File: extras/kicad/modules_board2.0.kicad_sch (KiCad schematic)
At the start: 31 parts, among them J1 CONN_08NO_SILK_FEMALE_PTH, J10 CONN_06LOCK, J12 CONN_06LOCK, J13 CONN_06LOCK, J2 CONN_08NO_SILK_FEMALE_PTH, J3 CONN_08NO_SILK_FEMALE_PTH, J4 CONN_08NO_SILK_FEMALE_PTH, J9 CONN_06LOCK

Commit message: Add files via upload
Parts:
- removed J10, J12, J13, J9: CONN_06LOCK, modules_board:1X06_LOCK, symbol modules_board-eagle-import:CONN_06LOCK
- removed J?: UEXT_Slave, symbol Connector:UEXT_Slave
- removed UNK5V_REGULATOR0: CONN_03LOCK, modules_board:1X03_LOCK, symbol modules_board-eagle-import:CONN_03LOCK
- added J?: Conn_02x08_Odd_Even, symbol Connector_Generic:Conn_02x08_Odd_Even
- added J? (x4): Conn_01x04_Male, symbol Connector:Conn_01x04_Male
- added J? (x5): Conn_01x05_Male, symbol Connector:Conn_01x05_Male
- added J?: Conn_01x07_Male, symbol Connector:Conn_01x07_Male
- added J?: UEXT_Slave, symbol Connector:UEXT_Slave
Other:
- note added: "3amp @5v"
- note added: "Breakout garden SPI"
- note added: "Featherwing Breakout - UART I2C & SPI"
- note added: "Grove I2C"
- note added: "Qwiic I2C"
- note added: "https://shop.pimoroni.com/collections/breakout-garden"
- note added: "https://www.adafruit.com/category/573"
- note added: "https://www.mikroe.com/mikrobus-shuttle-127mm-2x8-pin-box-header-smd-male"
- note added: "mikroMOD"

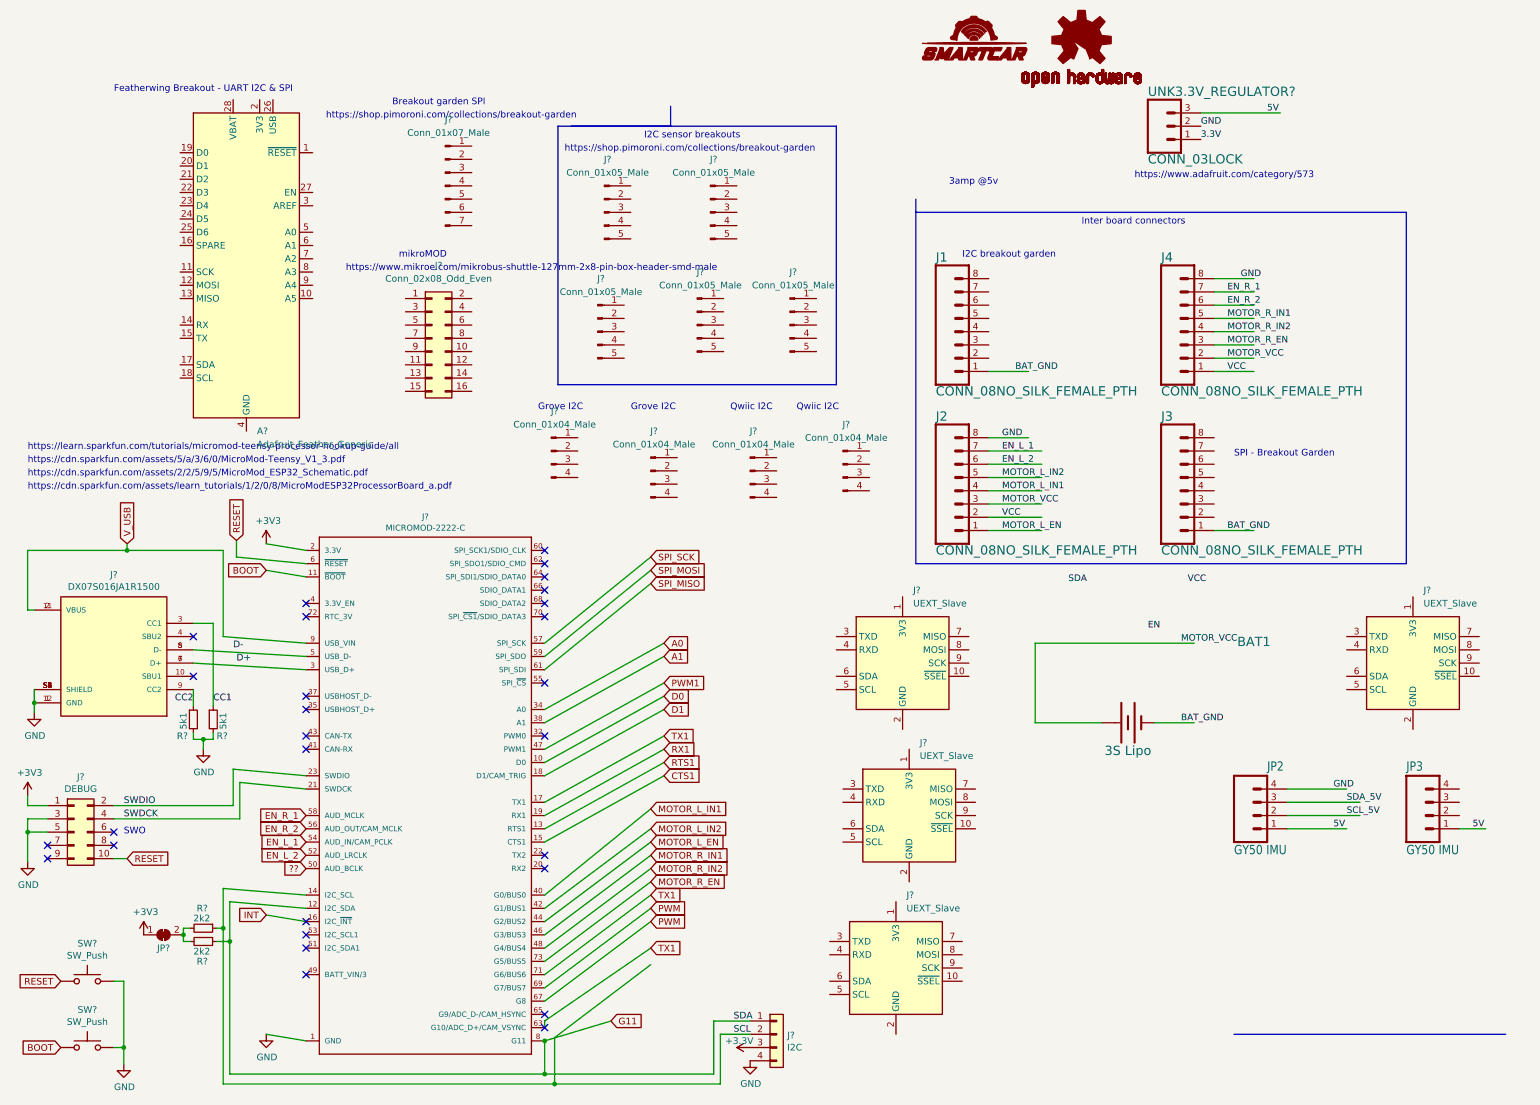
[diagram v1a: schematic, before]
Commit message: Add BNO-85
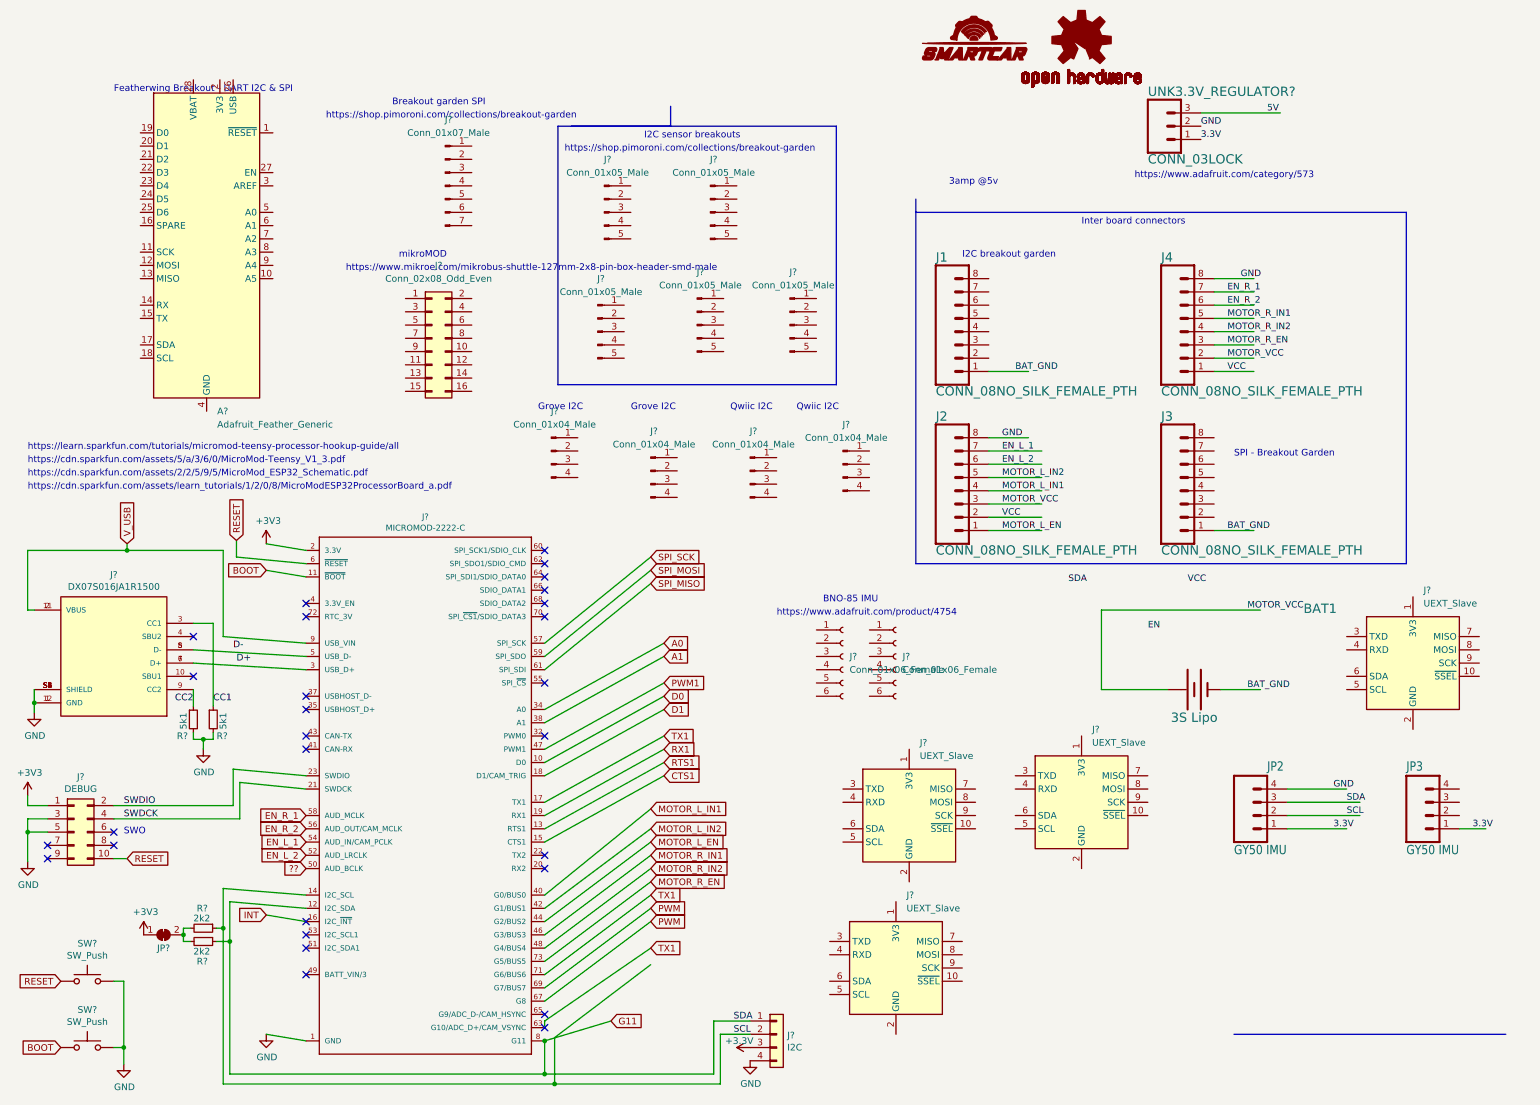
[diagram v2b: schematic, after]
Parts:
- added J? (x2): Conn_01x06_Female, symbol Connector:Conn_01x06_Female
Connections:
- net SCL_5V is gone; now on net SCL: JP2.2
- net SDA_5V is gone; now on net G11: JP2.3
- net +3V3: now also JP2.1, JP3.1
- net 5V: no longer JP2.1, JP3.1
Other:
- note added: "BNO-85 IMU"
- note added: "https://www.adafruit.com/product/4754"
- moved on the sheet: A?, BAT1, J?
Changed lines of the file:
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@@
     (stroke (width 0) (type default) (color 0 0 0 0))
   )
-  (wire (pts (xy 207.01 135.89) (xy 219.71 135.89))
+  (wire (pts (xy 219.71 129.54) (xy 232.41 129.54))
     (stroke (width 0) (type default) (color 0 0 0 0))
   )
@@
     (stroke (width 0) (type default) (color 0 0 0 0))
   )
-  (wire (pts (xy 207.01 120.65) (xy 237.49 120.65))
+  (wire (pts (xy 219.71 114.3) (xy 250.19 114.3))
     (stroke (width 0) (type default) (color 0 0 0 0))
   )
@@
     (stroke (width 0) (type default) (color 0 0 0 0))
   )
-  (wire (pts (xy 229.87 135.89) (xy 237.49 135.89))
+  (wire (pts (xy 242.57 129.54) (xy 250.19 129.54))
     (stroke (width 0) (type default) (color 0 0 0 0))
   )
@@
     (stroke (width 0) (type default) (color 0 0 0 0))
   )
-  (wire (pts (xy 207.01 120.65) (xy 207.01 135.89))
+  (wire (pts (xy 219.71 114.3) (xy 219.71 129.54))
     (stroke (width 0) (type default) (color 0 0 0 0))
   )
@@
     (effects (font (size 1.27 1.27)) (justify left bottom))
   )
+  (text "BNO-85 IMU" (at 166.37 113.03 0)
+    (effects (font (size 1.27 1.27)) (justify left bottom))
+  )
   (text "Inter board connectors" (at 215.9 40.64 0)
     (effects (font (size 1.27 1.27)) (justify left bottom))
@@
     (effects (font (size 1.27 1.27)) (justify left bottom))
   )
+  (text "https://www.adafruit.com/product/4754" (at 157.48 115.57 0)
+    (effects (font (size 1.27 1.27)) (justify left bottom))
+  )
   (label "VCC" (at 236.22 109.22 0)
     (effects (font (size 1.2446 1.2446)) (justify left bottom))
@@
     (effects (font (size 1.2446 1.2446)) (justify left bottom))
   )
-  (label "SDA_5V" (at 266.7 151.13 0)
+  (label "SDA" (at 266.7 151.13 0)
     (effects (font (size 1.2446 1.2446)) (justify left bottom))
   )
@@
     (effects (font (size 1.27 1.27)) (justify left bottom))
   )
-  (label "5V" (at 264.16 156.21 0)
+  (label "3.3V" (at 264.16 156.21 0)
     (effects (font (size 1.2446 1.2446)) (justify left bottom))
   )
@@
     (effects (font (size 1.2446 1.2446)) (justify left bottom))
   )
-  (label "BAT_GND" (at 234.95 135.89 0)
-    (effects (font (size 1.2446 1.2446)) (justify left bottom))
-  )
-  (label "5V" (at 290.83 156.21 0)
+  (label "BAT_GND" (at 247.65 129.54 0)
+    (effects (font (size 1.2446 1.2446)) (justify left bottom))
+  )
+  (label "3.3V" (at 290.83 156.21 0)
     (effects (font (size 1.2446 1.2446)) (justify left bottom))
   )
@@
     (effects (font (size 1.2446 1.2446)) (justify left bottom))
   )
-  (label "MOTOR_VCC" (at 234.95 120.65 0)
+  (label "MOTOR_VCC" (at 247.65 114.3 0)
     (effects (font (size 1.2446 1.2446)) (justify left bottom))
   )
@@
     (effects (font (size 1.27 1.27)) (justify right bottom))
   )
-  (label "SCL_5V" (at 266.7 153.67 0)
+  (label "SCL" (at 266.7 153.67 0)
     (effects (font (size 1.2446 1.2446)) (justify left bottom))
   )
@@
     )
   )
-  (symbol (lib_id "modules_board-eagle-import:AA-BATTERY-PTH") (at 224.79 135.89 0) (unit 1)
-    (in_bom yes) (on_board yes)
-    (property "Reference" "BAT1" (id 0) (at 248.92 121.412 0)
+  (symbol (lib_id "modules_board-eagle-import:AA-BATTERY-PTH") (at 237.49 129.54 0) (unit 1)
+    (in_bom yes) (on_board yes)
+    (property "Reference" "BAT1" (id 0) (at 261.62 115.062 0)
       (effects (font (size 1.778 1.778)) (justify bottom))
     )
-    (property "Value" "3S Lipo" (id 1) (at 224.79 140.208 0)
+    (property "Value" "3S Lipo" (id 1) (at 237.49 133.858 0)
       (effects (font (size 1.778 1.778)) (justify top))
     )
-    (property "Footprint" "modules_board:AA-PCB-BATTERY" (id 2) (at 224.79 135.89 0)
-      (effects (font (size 1.27 1.27)) hide)
-    )
-    (property "Datasheet" "" (id 3) (at 224.79 135.89 0)
+    (property "Footprint" "modules_board:AA-PCB-BATTERY" (id 2) (at 237.49 129.54 0)
+      (effects (font (size 1.27 1.27)) hide)
+    )
+    (property "Datasheet" "" (id 3) (at 237.49 129.54 0)
       (effects (font (size 1.27 1.27)) hide)
     )
@@
     (pin "S6")
   )
-  (symbol (lib_id "Connector:UEXT_Slave") (at 181.61 124.46 0) (unit 1)
+  (symbol (lib_id "Connector:UEXT_Slave") (at 215.9 151.13 0) (unit 1)
     (in_bom yes) (on_board yes) (fields_autoplaced)
-    (property "Reference" "J?" (id 0) (at 183.6294 110.49 0)
-      (effects (font (size 1.27 1.27)) (justify left))
-    )
-    (property "Value" "UEXT_Slave" (id 1) (at 183.6294 113.03 0)
-      (effects (font (size 1.27 1.27)) (justify left))
-    )
-    (property "Footprint" "" (id 2) (at 177.8 124.46 0)
-      (effects (font (size 1.27 1.27)) hide)
-    )
-    (property "Datasheet" "https://www.olimex.com/Products/Modules/UEXT/resources/UEXT_rev_B.pdf" (id 3) (at 177.8 124.46 0)
+    (property "Reference" "J?" (id 0) (at 217.9194 137.16 0)
+      (effects (font (size 1.27 1.27)) (justify left))
+    )
+    (property "Value" "UEXT_Slave" (id 1) (at 217.9194 139.7 0)
+      (effects (font (size 1.27 1.27)) (justify left))
+    )
+    (property "Footprint" "" (id 2) (at 212.09 151.13 0)
+      (effects (font (size 1.27 1.27)) hide)
+    )
+    (property "Datasheet" "https://www.olimex.com/Products/Modules/UEXT/resources/UEXT_rev_B.pdf" (id 3) (at 212.09 151.13 0)
       (effects (font (size 1.27 1.27)) hide)
     )
@@
     (pin "1")
     (pin "2")
+  )
+  (symbol (lib_id "Connector:Conn_01x06_Female") (at 170.18 123.19 0) (unit 1)
+    (in_bom yes) (on_board yes) (fields_autoplaced)
+    (property "Reference" "J?" (id 0) (at 171.45 123.1899 0)
+      (effects (font (size 1.27 1.27)) (justify left))
+    )
+    (property "Value" "Conn_01x06_Female" (id 1) (at 171.45 125.7299 0)
+      (effects (font (size 1.27 1.27)) (justify left))
+    )
+    (property "Footprint" "" (id 2) (at 170.18 123.19 0)
+      (effects (font (size 1.27 1.27)) hide)
+    )
+    (property "Datasheet" "~" (id 3) (at 170.18 123.19 0)
+      (effects (font (size 1.27 1.27)) hide)
+    )
+    (pin "1")
+    (pin "2")
+    (pin "3")
+    (pin "4")
+    (pin "5")
+    (pin "6")
   )
   (symbol (lib_id "Connector:UEXT_Slave") (at 182.88 153.67 0) (unit 1)
@@
     (pin "2")
   )
-  (symbol (lib_id "MCU_Module:Adafruit_Feather_Generic") (at 55.88 46.99 0) (unit 1)
+  (symbol (lib_id "MCU_Module:Adafruit_Feather_Generic") (at 48.26 43.18 0) (unit 1)
     (in_bom yes) (on_board yes) (fields_autoplaced)
-    (property "Reference" "A?" (id 0) (at 57.8994 80.01 0)
-      (effects (font (size 1.27 1.27)) (justify left))
-    )
-    (property "Value" "Adafruit_Feather_Generic" (id 1) (at 57.8994 82.55 0)
-      (effects (font (size 1.27 1.27)) (justify left))
-    )
-    (property "Footprint" "Module:Adafruit_Feather" (id 2) (at 58.42 81.28 0)
+    (property "Reference" "A?" (id 0) (at 50.2794 76.2 0)
+      (effects (font (size 1.27 1.27)) (justify left))
+    )
+    (property "Value" "Adafruit_Feather_Generic" (id 1) (at 50.2794 78.74 0)
+      (effects (font (size 1.27 1.27)) (justify left))
+    )
+    (property "Footprint" "Module:Adafruit_Feather" (id 2) (at 50.8 77.47 0)
       (effects (font (size 1.27 1.27)) (justify left) hide)
     )
-    (property "Datasheet" "https://cdn-learn.adafruit.com/downloads/pdf/adafruit-feather.pdf" (id 3) (at 55.88 67.31 0)
+    (property "Datasheet" "https://cdn-learn.adafruit.com/downloads/pdf/adafruit-feather.pdf" (id 3) (at 48.26 63.5 0)
       (effects (font (size 1.27 1.27)) hide)
     )
@@
     (pin "1")
   )
+  (symbol (lib_id "Connector:Conn_01x06_Female") (at 180.34 123.19 0) (unit 1)
+    (in_bom yes) (on_board yes) (fields_autoplaced)
+    (property "Reference" "J?" (id 0) (at 181.61 123.1899 0)
+      (effects (font (size 1.27 1.27)) (justify left))
+    )
+    (property "Value" "Conn_01x06_Female" (id 1) (at 181.61 125.7299 0)
+      (effects (font (size 1.27 1.27)) (justify left))
+    )
+    (property "Footprint" "" (id 2) (at 180.34 123.19 0)
+      (effects (font (size 1.27 1.27)) hide)
+    )
+    (property "Datasheet" "~" (id 3) (at 180.34 123.19 0)
+      (effects (font (size 1.27 1.27)) hide)
+    )
+    (pin "1")
+    (pin "2")
+    (pin "3")
+    (pin "4")
+    (pin "5")
+    (pin "6")
+  )
   (symbol (lib_id "Connector:UEXT_Slave") (at 279.4 124.46 0) (unit 1)
     (in_bom yes) (on_board yes) (fields_autoplaced)
@@
       (reference "J?") (unit 1) (value "DEBUG") (footprint "Connector_PinHeader_1.27mm:PinHeader_2x05_P1.27mm_Vertical")
     )
+    (path "/4cee0ce4-6fc7-4759-b2b2-e85394e31440"
+      (reference "J?") (unit 1) (value "Conn_01x06_Female") (footprint "")
+    )
     (path "/53a48db4-c2e5-4b37-8d73-4c5f9025a664"
       (reference "J?") (unit 1) (value "UEXT_Slave") (footprint "")
@@
       (reference "J?") (unit 1) (value "Conn_01x07_Male") (footprint "")
     )
+    (path "/9b8a97f3-3490-47d4-8ad2-5272108ae8a7"
+      (reference "J?") (unit 1) (value "Conn_01x06_Female") (footprint "")
+    )
     (path "/a2ff99fe-a37d-4573-a1bd-e223eba6e852"
